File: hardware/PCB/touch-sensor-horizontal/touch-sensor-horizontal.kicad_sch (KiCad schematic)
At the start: 1 part

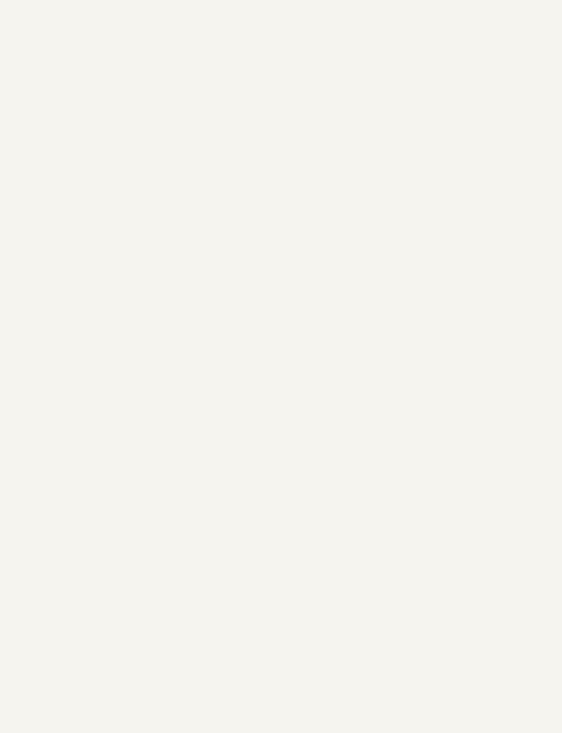
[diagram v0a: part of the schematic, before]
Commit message: removed dropped ideas, re organised datasheets, created project for integrated touch sensor
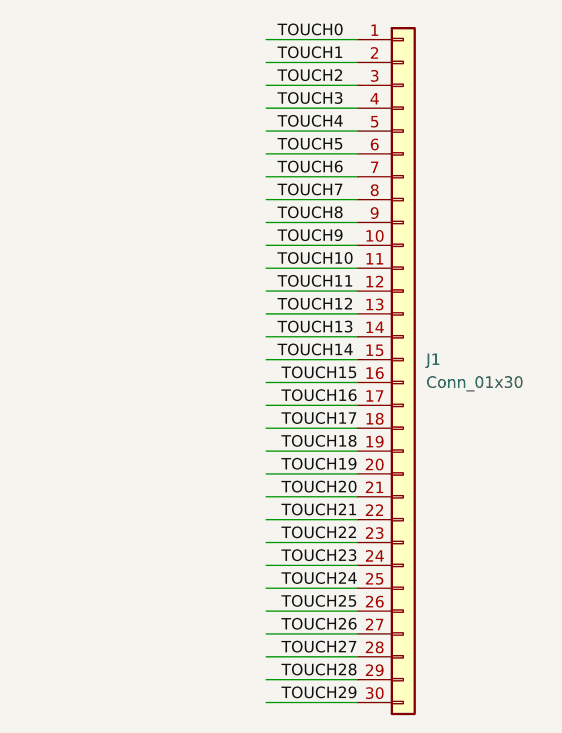
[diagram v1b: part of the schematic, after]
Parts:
- added J1: Conn_01x30, touch-sensors:tstick-buttons, symbol Connector_Generic:Conn_01x30
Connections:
- net TOUCH0: now also J1.1 (Pin_1)
- net TOUCH1: now also J1.2 (Pin_2)
- net TOUCH10: now also J1.11 (Pin_11)
- net TOUCH11: now also J1.12 (Pin_12)
- net TOUCH12: now also J1.13 (Pin_13)
- net TOUCH13: now also J1.14 (Pin_14)
- net TOUCH14: now also J1.15 (Pin_15)
- net TOUCH15: now also J1.16 (Pin_16)
- net TOUCH16: now also J1.17 (Pin_17)
- net TOUCH17: now also J1.18 (Pin_18)
- net TOUCH18: now also J1.19 (Pin_19)
- net TOUCH19: now also J1.20 (Pin_20)
- net TOUCH2: now also J1.3 (Pin_3)
- net TOUCH20: now also J1.21 (Pin_21)
- net TOUCH21: now also J1.22 (Pin_22)
- net TOUCH22: now also J1.23 (Pin_23)
- net TOUCH23: now also J1.24 (Pin_24)
- net TOUCH24: now also J1.25 (Pin_25)
- net TOUCH25: now also J1.26 (Pin_26)
- net TOUCH26: now also J1.27 (Pin_27)
- net TOUCH27: now also J1.28 (Pin_28)
- net TOUCH28: now also J1.29 (Pin_29)
- net TOUCH29: now also J1.30 (Pin_30)
- net TOUCH3: now also J1.4 (Pin_4)
- net TOUCH4: now also J1.5 (Pin_5)
- net TOUCH5: now also J1.6 (Pin_6)
- net TOUCH6: now also J1.7 (Pin_7)
- net TOUCH7: now also J1.8 (Pin_8)
- net TOUCH8: now also J1.9 (Pin_9)
- net TOUCH9: now also J1.10 (Pin_10)

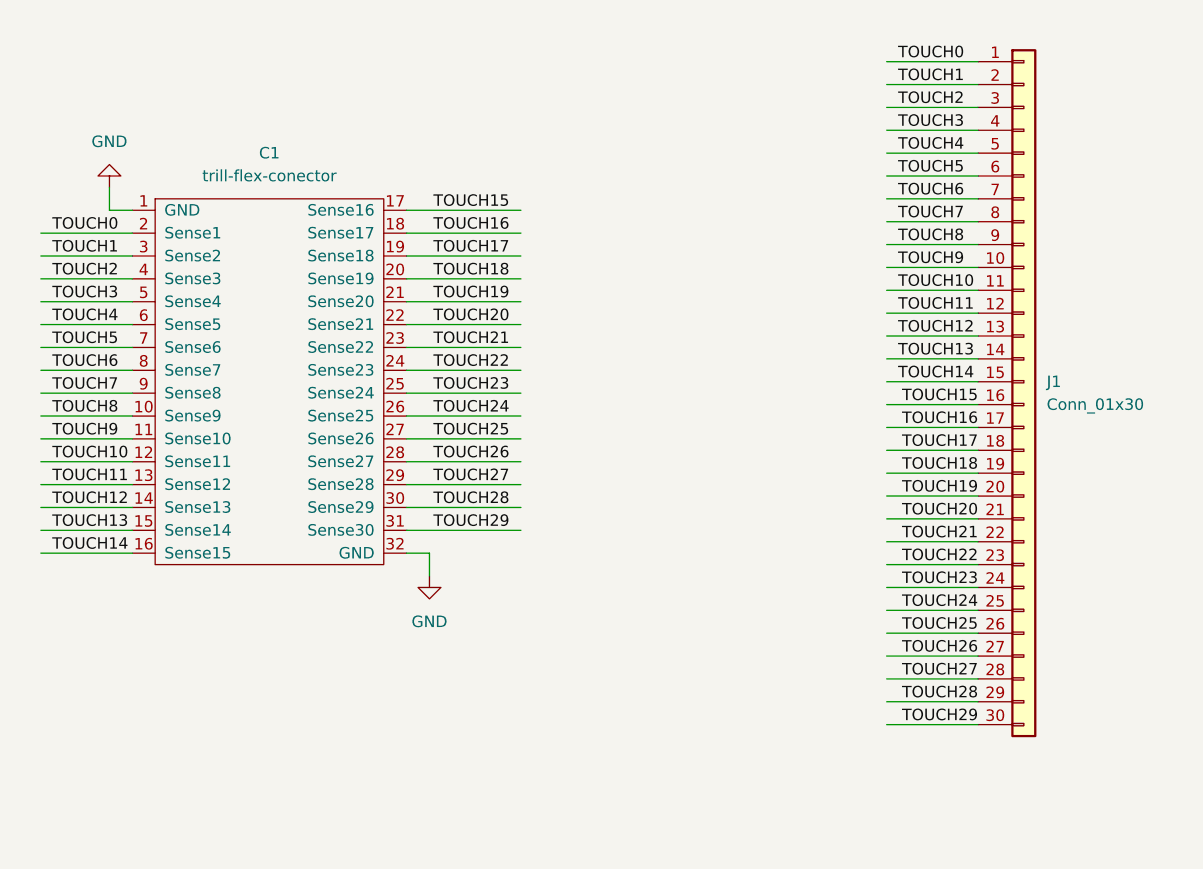
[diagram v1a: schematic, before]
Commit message: updated touch sensor design to be at the end of the board, also has longer neck
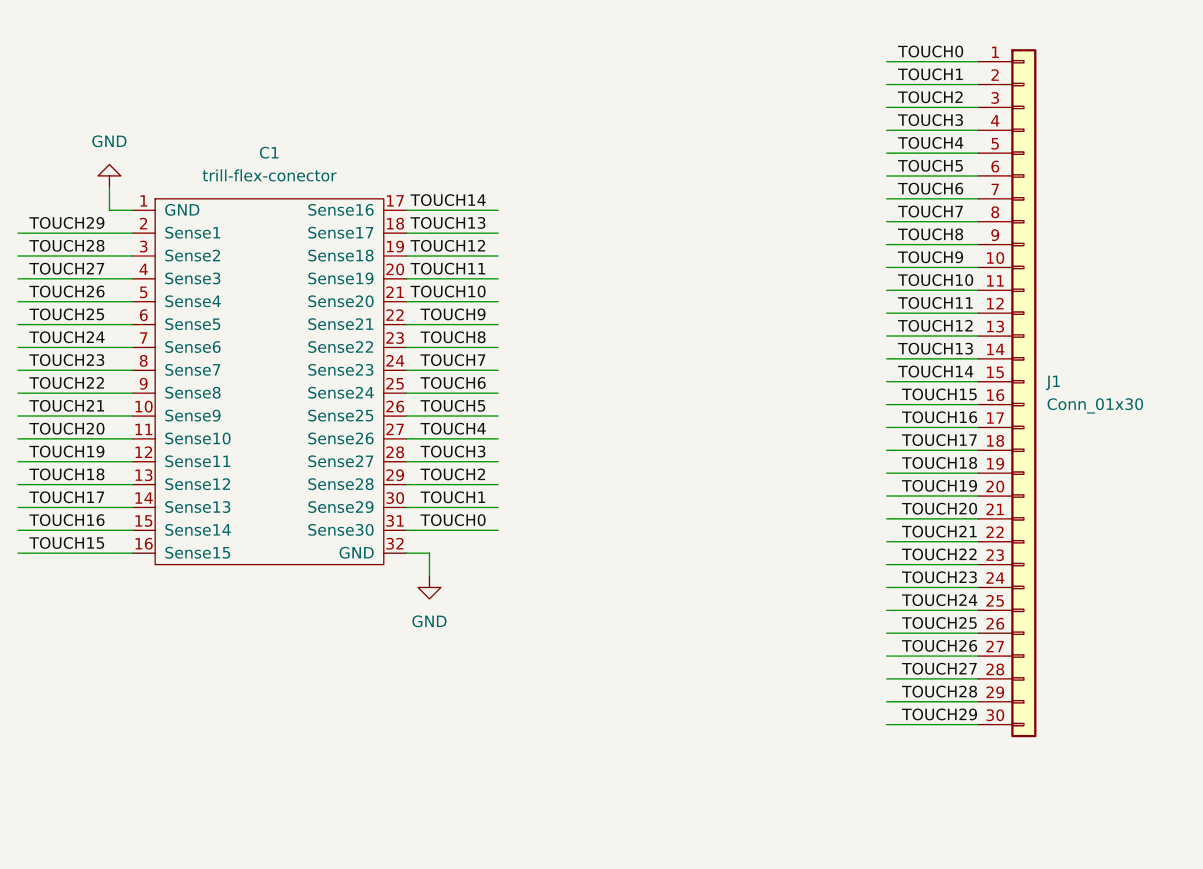
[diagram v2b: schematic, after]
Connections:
- net TOUCH0: now also C1.31 (Sense30); no longer C1.2 (Sense1)
- net TOUCH1: now also C1.30 (Sense29); no longer C1.3 (Sense2)
- net TOUCH10: now also C1.21 (Sense20); no longer C1.12 (Sense11)
- net TOUCH11: now also C1.20 (Sense19); no longer C1.13 (Sense12)
- net TOUCH12: now also C1.19 (Sense18); no longer C1.14 (Sense13)
- net TOUCH13: now also C1.18 (Sense17); no longer C1.15 (Sense14)
- net TOUCH14: now also C1.17 (Sense16); no longer C1.16 (Sense15)
- net TOUCH15: now also C1.16 (Sense15); no longer C1.17 (Sense16)
- net TOUCH16: now also C1.15 (Sense14); no longer C1.18 (Sense17)
- net TOUCH17: now also C1.14 (Sense13); no longer C1.19 (Sense18)
- net TOUCH18: now also C1.13 (Sense12); no longer C1.20 (Sense19)
- net TOUCH19: now also C1.12 (Sense11); no longer C1.21 (Sense20)
- net TOUCH2: now also C1.29 (Sense28); no longer C1.4 (Sense3)
- net TOUCH20: now also C1.11 (Sense10); no longer C1.22 (Sense21)
- net TOUCH21: now also C1.10 (Sense9); no longer C1.23 (Sense22)
- net TOUCH22: now also C1.9 (Sense8); no longer C1.24 (Sense23)
- net TOUCH23: now also C1.8 (Sense7); no longer C1.25 (Sense24)
- net TOUCH24: now also C1.7 (Sense6); no longer C1.26 (Sense25)
- net TOUCH25: now also C1.6 (Sense5); no longer C1.27 (Sense26)
- net TOUCH26: now also C1.5 (Sense4); no longer C1.28 (Sense27)
- net TOUCH27: now also C1.4 (Sense3); no longer C1.29 (Sense28)
- net TOUCH28: now also C1.3 (Sense2); no longer C1.30 (Sense29)
- net TOUCH29: now also C1.2 (Sense1); no longer C1.31 (Sense30)
- net TOUCH3: now also C1.28 (Sense27); no longer C1.5 (Sense4)
- net TOUCH4: now also C1.27 (Sense26); no longer C1.6 (Sense5)
- net TOUCH5: now also C1.26 (Sense25); no longer C1.7 (Sense6)
- net TOUCH6: now also C1.25 (Sense24); no longer C1.8 (Sense7)
- net TOUCH7: now also C1.24 (Sense23); no longer C1.9 (Sense8)
- net TOUCH8: now also C1.23 (Sense22); no longer C1.10 (Sense9)
- net TOUCH9: now also C1.22 (Sense21); no longer C1.11 (Sense10)

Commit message: updated touch sensor design to be a slider
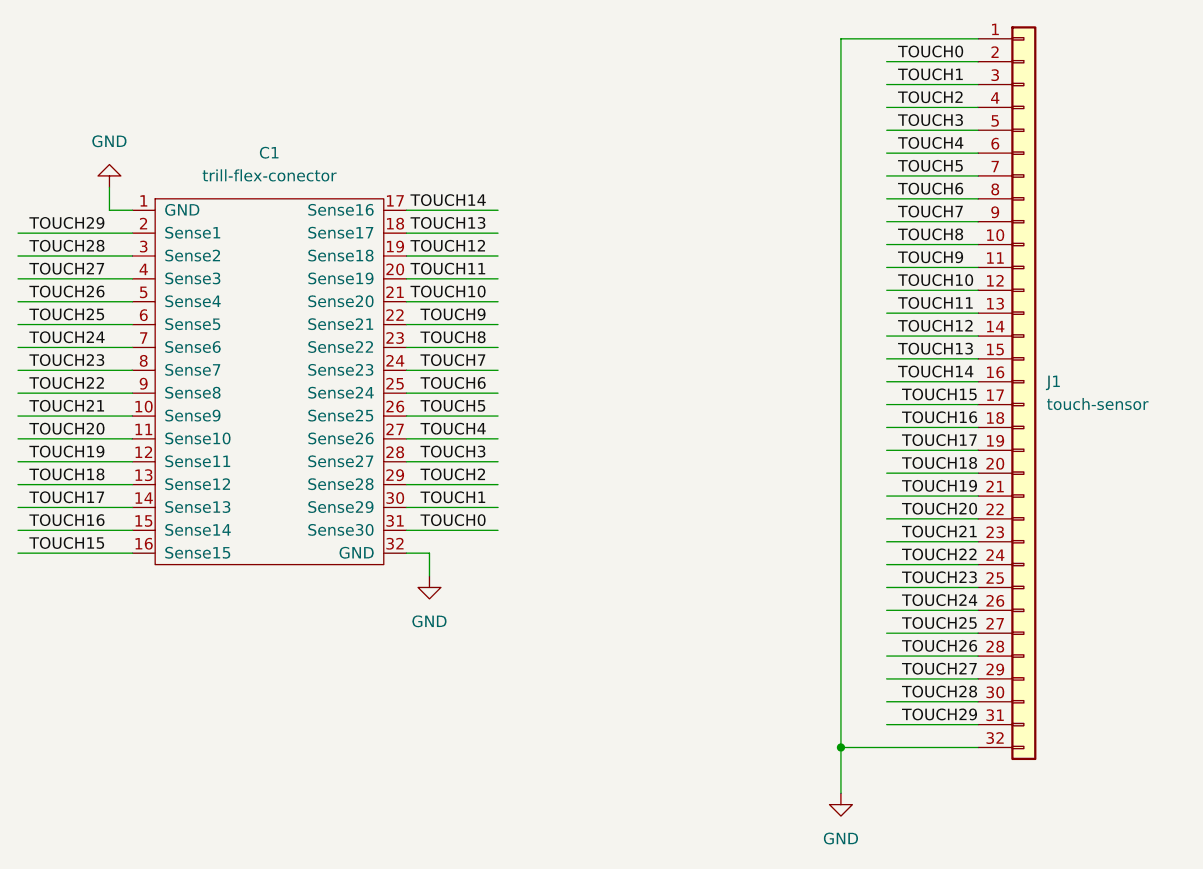
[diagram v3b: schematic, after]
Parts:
- J1: value Conn_01x30 -> touch-sensor; footprint touch-sensors:tstick-buttons -> touch-sensors:tstick-slider; symbol Connector_Generic:Conn_01x30 -> Connector_Generic:Conn_01x32
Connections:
- net GND: now also J1.1 (Pin_1), J1.32 (Pin_32)
- net TOUCH0: now also J1.2 (Pin_2); no longer J1.1 (Pin_1)
- net TOUCH1: now also J1.3 (Pin_3); no longer J1.2 (Pin_2)
- net TOUCH10: now also J1.12 (Pin_12); no longer J1.11 (Pin_11)
- net TOUCH11: now also J1.13 (Pin_13); no longer J1.12 (Pin_12)
- net TOUCH12: now also J1.14 (Pin_14); no longer J1.13 (Pin_13)
- net TOUCH13: now also J1.15 (Pin_15); no longer J1.14 (Pin_14)
- net TOUCH14: now also J1.16 (Pin_16); no longer J1.15 (Pin_15)
- net TOUCH15: now also J1.17 (Pin_17); no longer J1.16 (Pin_16)
- net TOUCH16: now also J1.18 (Pin_18); no longer J1.17 (Pin_17)
- net TOUCH17: now also J1.19 (Pin_19); no longer J1.18 (Pin_18)
- net TOUCH18: now also J1.20 (Pin_20); no longer J1.19 (Pin_19)
- net TOUCH19: now also J1.21 (Pin_21); no longer J1.20 (Pin_20)
- net TOUCH2: now also J1.4 (Pin_4); no longer J1.3 (Pin_3)
- net TOUCH20: now also J1.22 (Pin_22); no longer J1.21 (Pin_21)
- net TOUCH21: now also J1.23 (Pin_23); no longer J1.22 (Pin_22)
- net TOUCH22: now also J1.24 (Pin_24); no longer J1.23 (Pin_23)
- net TOUCH23: now also J1.25 (Pin_25); no longer J1.24 (Pin_24)
- net TOUCH24: now also J1.26 (Pin_26); no longer J1.25 (Pin_25)
- net TOUCH25: now also J1.27 (Pin_27); no longer J1.26 (Pin_26)
- net TOUCH26: now also J1.28 (Pin_28); no longer J1.27 (Pin_27)
- net TOUCH27: now also J1.29 (Pin_29); no longer J1.28 (Pin_28)
- net TOUCH28: now also J1.30 (Pin_30); no longer J1.29 (Pin_29)
- net TOUCH29: now also J1.31 (Pin_31); no longer J1.30 (Pin_30)
- net TOUCH3: now also J1.5 (Pin_5); no longer J1.4 (Pin_4)
- net TOUCH4: now also J1.6 (Pin_6); no longer J1.5 (Pin_5)
- net TOUCH5: now also J1.7 (Pin_7); no longer J1.6 (Pin_6)
- net TOUCH6: now also J1.8 (Pin_8); no longer J1.7 (Pin_7)
- net TOUCH7: now also J1.9 (Pin_9); no longer J1.8 (Pin_8)
- net TOUCH8: now also J1.10 (Pin_10); no longer J1.9 (Pin_9)
- net TOUCH9: now also J1.11 (Pin_11); no longer J1.10 (Pin_10)
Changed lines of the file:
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@@
 (kicad_sch (version 20230121) (generator eeschema)
   (paper "A4")
+  (junction (at 143.51 121.92) (diameter 0) (color 0 0 0 0)
+  )
   (wire (pts (xy 148.59 91.44) (xy 158.75 91.44))
     (stroke (width 0) (type default))
@@
     (stroke (width 0) (type default))
   )
+  (wire (pts (xy 143.51 121.92) (xy 158.75 121.92))
+    (stroke (width 0) (type default))
+  )
+  (wire (pts (xy 158.75 43.18) (xy 143.51 43.18))
+    (stroke (width 0) (type default))
+  )
   (wire (pts (xy 105.41 82.55) (xy 95.25 82.55))
     (stroke (width 0) (type default))
@@
     (stroke (width 0) (type default))
   )
+  (wire (pts (xy 143.51 43.18) (xy 143.51 121.92))
+    (stroke (width 0) (type default))
+  )
   (wire (pts (xy 105.41 72.39) (xy 95.25 72.39))
     (stroke (width 0) (type default))
@@
     (stroke (width 0) (type default))
   )
+  (wire (pts (xy 143.51 121.92) (xy 143.51 127))
+    (stroke (width 0) (type default))
+  )
   (wire (pts (xy 148.59 101.6) (xy 158.75 101.6))
     (stroke (width 0) (type default))
@@
   (label "TOUCH17" (at 53.34 95.25 0) (fields_autoplaced)
     (effects (font (size 1.27 1.27)) (justify left bottom))
+  )
+  (symbol (lib_id "power:GND") (at 143.51 127 0) (unit 1)
+    (in_bom yes) (on_board yes) (dnp no) (fields_autoplaced)
+    (property "Reference" "#PWR03" (at 143.51 133.35 0)
+      (effects (font (size 1.27 1.27)) hide)
+    )
+    (property "Value" "GND" (at 143.51 132.08 0)
+      (effects (font (size 1.27 1.27)))
+    )
+    (property "Footprint" "" (at 143.51 127 0)
+      (effects (font (size 1.27 1.27)) hide)
+    )
+    (property "Datasheet" "" (at 143.51 127 0)
+      (effects (font (size 1.27 1.27)) hide)
+    )
+    (pin "1")
+    (instances
+      (project "touch-sensor-horizontal"
+        (path "/beaa8ee0-3ec8-40a6-99fa-0f4d6fddebd1"
+          (reference "#PWR03") (unit 1)
+        )
+      )
+    )
   )
   (symbol (lib_id "trill-flex:trill-flex-conector") (at 80.01 59.69 0) (unit 1)
@@
     )
   )
-  (symbol (lib_id "Connector_Generic:Conn_01x30") (at 163.83 81.28 0) (unit 1)
+  (symbol (lib_id "Connector_Generic:Conn_01x32") (at 163.83 81.28 0) (unit 1)
     (in_bom yes) (on_board yes) (dnp no) (fields_autoplaced)
     (property "Reference" "J1" (at 166.37 81.28 0)
       (effects (font (size 1.27 1.27)) (justify left))
     )
-    (property "Value" "Conn_01x30" (at 166.37 83.82 0)
+    (property "Value" "touch-sensor" (at 166.37 83.82 0)
       (effects (font (size 1.27 1.27)) (justify left))
     )
-    (property "Footprint" "touch-sensors:tstick-buttons" (at 163.83 81.28 0)
+    (property "Footprint" "touch-sensors:tstick-slider" (at 163.83 81.28 0)
       (effects (font (size 1.27 1.27)) hide)
     )
@@
     (pin "8")
     (pin "9")
+    (pin "31")
+    (pin "32")
     (instances
       (project "touch-sensor-horizontal"
